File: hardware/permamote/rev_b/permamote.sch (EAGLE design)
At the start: 124 parts, among them J1 TC2030-JLINK-NL, J5 MICRO_USB_B_HIROSE_ZX62R-B-5P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, Q1 PMDXB950UPEL, Q10 PMDXB950UPEL, Q2 PMDXB950UPEL, Q3 PMDXB950UPEL, Q4 PMDXB950UPEL, Q5 PMDXB950UPEL, Q6 PMDXB950UPEL, Q7 PMDXB950UPEL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

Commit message: add mpn, a few nits
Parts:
- R6, R7: value 10k -> DNP
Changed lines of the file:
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@@
 <?xml version="1.0" encoding="utf-8"?>
 <!DOCTYPE eagle SYSTEM "eagle.dtd">
-<eagle version="9.0.1">
+<eagle version="9.0.0">
 <drawing>
 <settings>
@@
 <attributes>
 <attribute name="AUTHOR" value="NEAL JACKSON"/>
-<attribute name="REV" value="A"/>
-<attribute name="TITLE" value="MOTE"/>
+<attribute name="REV" value="B"/>
+<attribute name="TITLE" value="PERMAMOTE"/>
 </attributes>
 <variantdefs>
@@
 </part>
 <part name="GND12" library="supply1" library_urn="urn:adsk.eagle:library:371" deviceset="GND" device=""/>
-<part name="R6" library="passives" deviceset="RESISTOR" device="0402_RES" value="10k">
+<part name="R6" library="passives" deviceset="RESISTOR" device="0402_RES" value="DNP">
 <attribute name="DIGIKEY" value="311-10KJRCT-ND "/>
 <attribute name="MPN" value="RC0402JR-0710KL"/>
@@
 <part name="P+8" library="supply1" library_urn="urn:adsk.eagle:library:371" deviceset="VCC" device=""/>
 <part name="P+1" library="supply1" library_urn="urn:adsk.eagle:library:371" deviceset="VCC" device=""/>
-<part name="R7" library="passives" deviceset="RESISTOR" device="0402_RES" value="10k">
+<part name="R7" library="passives" deviceset="RESISTOR" device="0402_RES" value="DNP">
 <attribute name="DIGIKEY" value="311-10KJRCT-ND "/>
 <attribute name="MPN" value="RC0402JR-0710KL"/>
@@
 <text x="185.42" y="101.6" size="1.778" layer="98">Note: Only populate one type of battery holder</text>
 <text x="2.54" y="182.88" size="5.08" layer="97">Power Supply</text>
-<wire x1="0" y1="68.58" x2="104.14" y2="68.58" width="0.254" layer="94" style="shortdash"/>
-<wire x1="104.14" y1="68.58" x2="104.14" y2="0" width="0.254" layer="94" style="shortdash"/>
+<wire x1="0" y1="71.12" x2="104.14" y2="71.12" width="0.254" layer="94" style="shortdash"/>
+<wire x1="104.14" y1="71.12" x2="104.14" y2="0" width="0.254" layer="94" style="shortdash"/>
 <text x="2.54" y="66.04" size="2.54" layer="97">Boost Regulator</text>
 <text x="124.46" y="53.34" size="1.778" layer="98" rot="R90" align="bottom-center">Divider for Lithium Titanate</text>

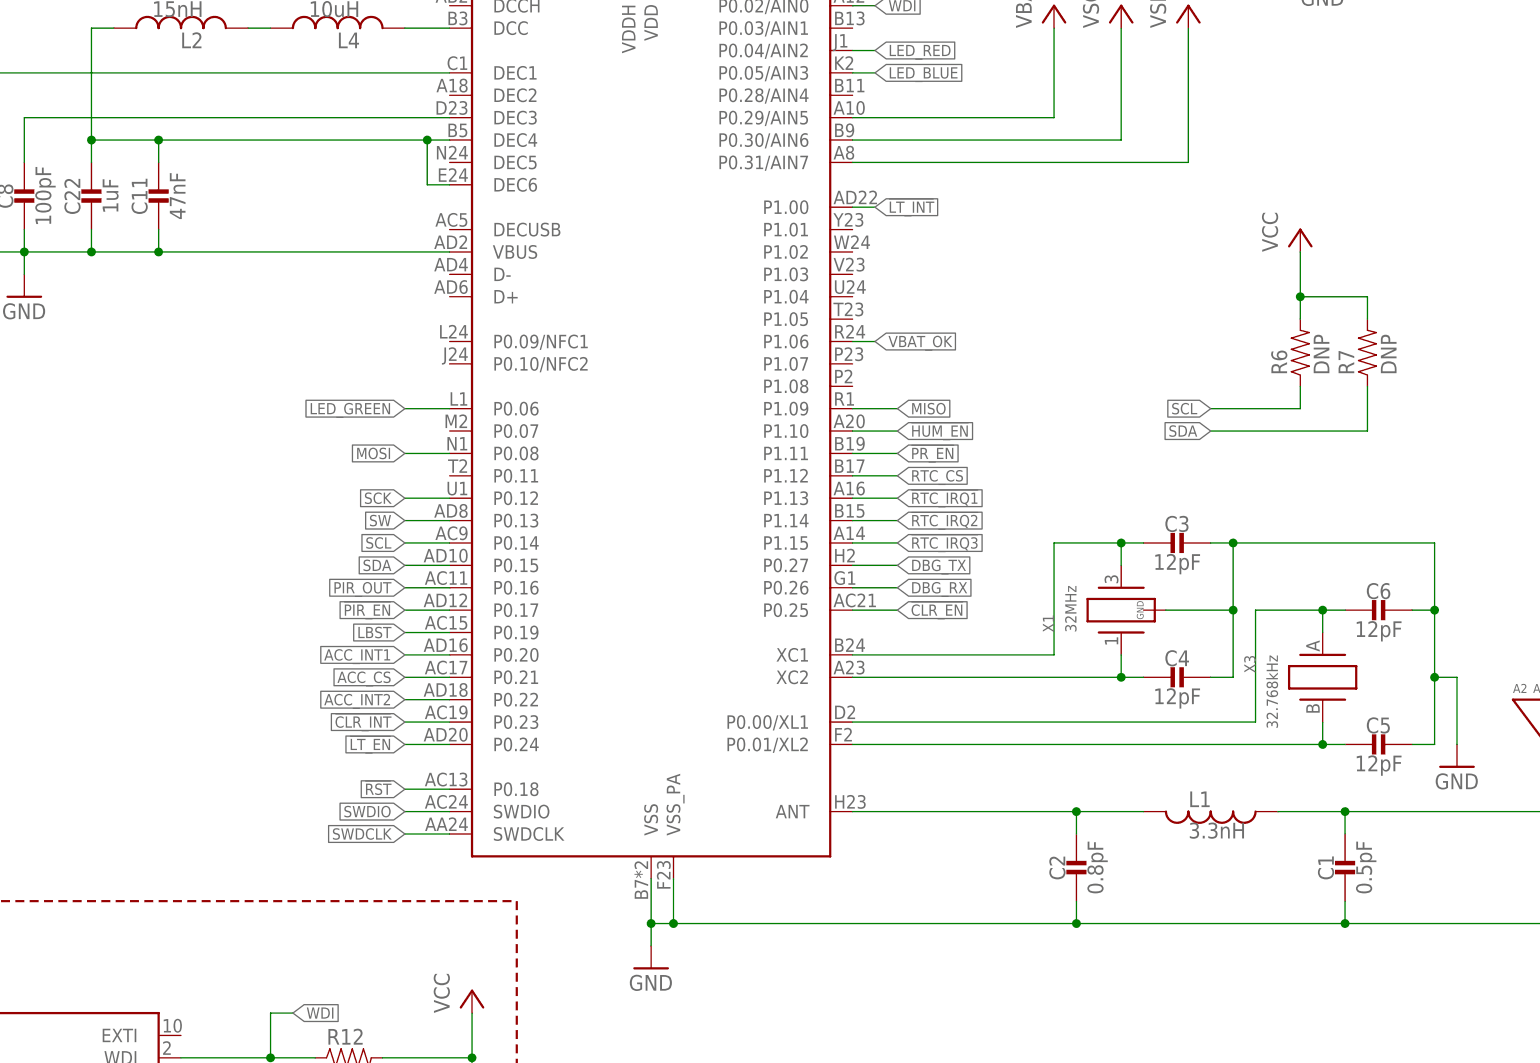
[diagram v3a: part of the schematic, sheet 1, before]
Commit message: Update to nrf52840 v1.0 spec
Add decoupling cap to DEC5
Change values of RF passives
mentioned in #3
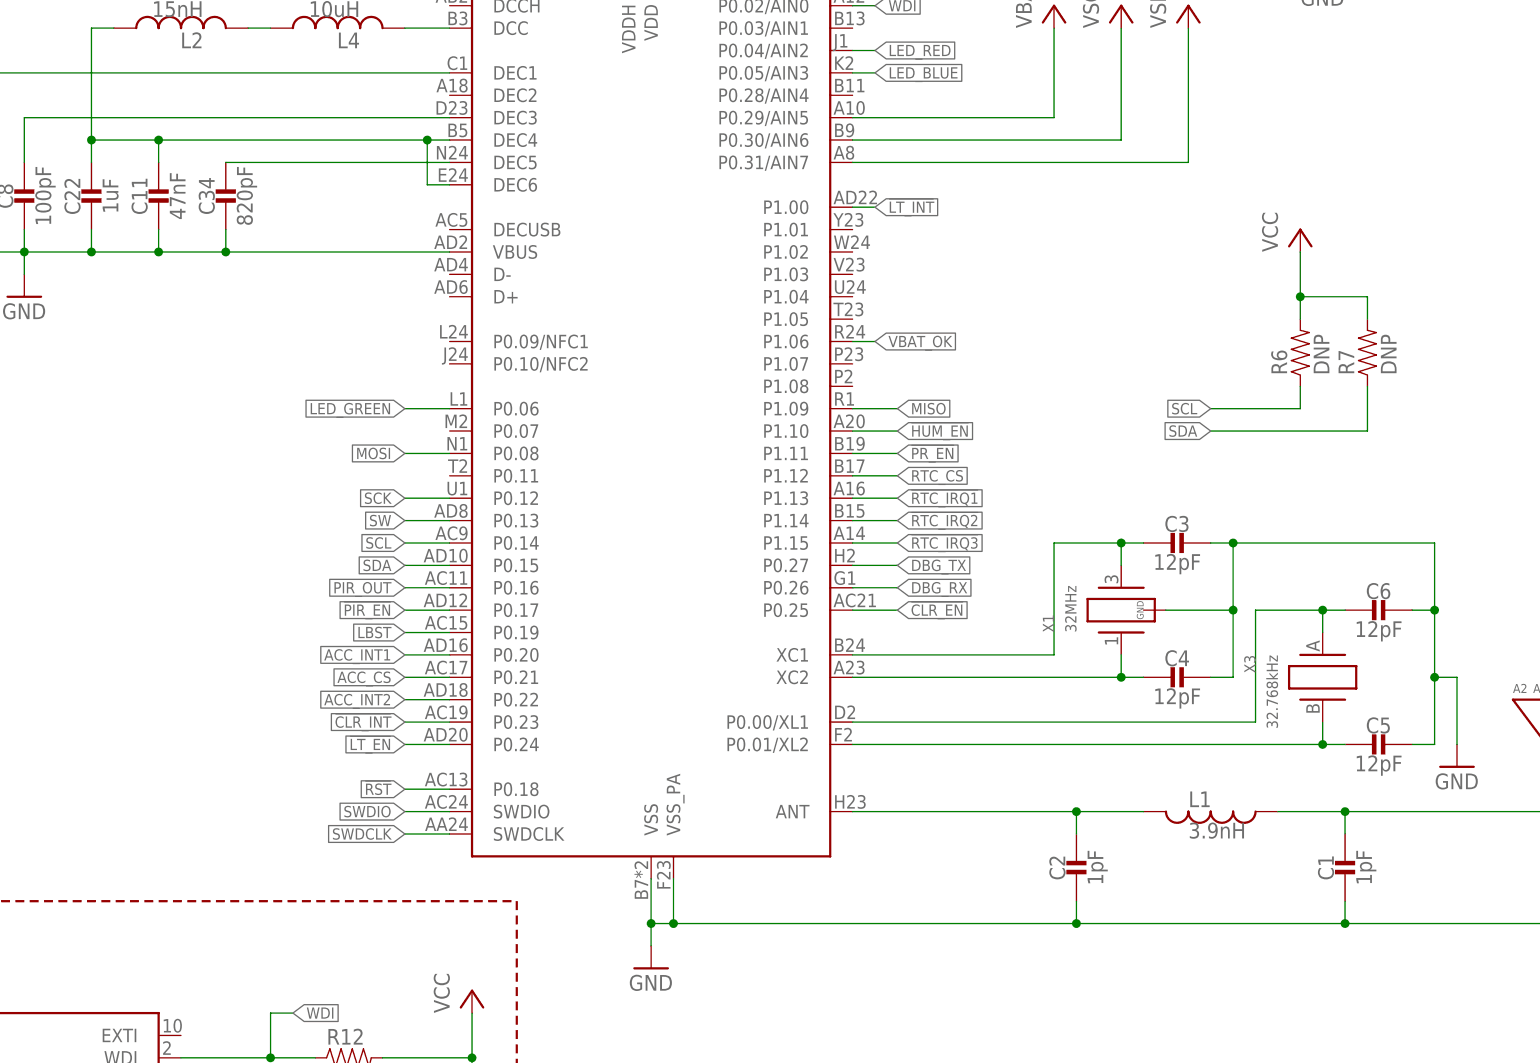
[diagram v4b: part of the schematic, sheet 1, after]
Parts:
- added C34: 820pF, passives:CAPACITOR0402_CAP
- C1: value 0.5pF -> 1pF; DIGIKEY 490-6264-1-ND -> 1276-1595-1-ND; MPN GRM1555C1HR50WA01D -> CL05C010CB5NNNC
- C2: value 0.8pF -> 1pF; DIGIKEY 490-6269-1-ND -> 1276-1595-1-ND; MPN GRM1555C1HR80BA01D -> CL05C010CB5NNNC
- L1: value 3.3nH -> 3.9nH; DIGIKEY 535-10426-1-ND -> 490-1131-1-ND; MPN AISC-0402-3N3J-T -> LQP15MN3N9B02D
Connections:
- new net N$1: C34.1, U10.DEC5
- net GND: now also C34.2
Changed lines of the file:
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@@
 <?xml version="1.0" encoding="utf-8"?>
 <!DOCTYPE eagle SYSTEM "eagle.dtd">
-<eagle version="9.0.0">
+<eagle version="9.0.1">
 <drawing>
 <settings>
@@
 <attribute name="MPN" value="GRM1555C1H120GA01D "/>
 </part>
-<part name="C2" library="passives" deviceset="CAPACITOR" device="0402_CAP" value="0.8pF">
-<attribute name="DIGIKEY" value="490-6269-1-ND"/>
-<attribute name="MPN" value="GRM1555C1HR80BA01D "/>
-</part>
-<part name="C1" library="passives" deviceset="CAPACITOR" device="0402_CAP" value="0.5pF">
-<attribute name="DIGIKEY" value="490-6264-1-ND"/>
-<attribute name="MPN" value="GRM1555C1HR50WA01D "/>
-</part>
-<part name="L1" library="passives" deviceset="INDUCTOR" device="0402" value="3.3nH">
-<attribute name="DIGIKEY" value="535-10426-1-ND"/>
-<attribute name="MPN" value="AISC-0402-3N3J-T "/>
+<part name="C2" library="passives" deviceset="CAPACITOR" device="0402_CAP" value="1pF">
+<attribute name="DIGIKEY" value="1276-1595-1-ND"/>
+<attribute name="MPN" value="CL05C010CB5NNNC"/>
+</part>
+<part name="C1" library="passives" deviceset="CAPACITOR" device="0402_CAP" value="1pF">
+<attribute name="DIGIKEY" value="1276-1595-1-ND"/>
+<attribute name="MPN" value="CL05C010CB5NNNC"/>
+</part>
+<part name="L1" library="passives" deviceset="INDUCTOR" device="0402" value="3.9nH">
+<attribute name="DIGIKEY" value="490-1131-1-ND"/>
+<attribute name="MPN" value="LQP15MN3N9B02D"/>
 </part>
 <part name="X1" library="crystals" deviceset="7V" device="-32.000MAHV-T" value="32MHz"/>
@@
 <part name="TP27" library="headers" deviceset="TEST-POINT" device=""/>
 <part name="U12" library="chips" deviceset="TCS34725" device=""/>
+<part name="C34" library="passives" deviceset="CAPACITOR" device="0402_CAP" value="820pF">
+<attribute name="DIGIKEY" value="1276-6535-1-ND"/>
+<attribute name="MPN" value="CL05B821KO5NNNC"/>
+</part>
 </parts>
 <sheets>
@@
 <instance part="P+16" gate="VCC" x="7.62" y="48.26"/>
 <instance part="P+18" gate="VCC" x="116.84" y="48.26"/>
+<instance part="C34" gate="G$1" x="88.9" y="139.7">
+<attribute name="DIGIKEY" x="88.9" y="139.7" size="1.778" layer="96" display="off"/>
+<attribute name="MPN" x="88.9" y="139.7" size="1.778" layer="96" display="off"/>
+</instance>
 </instances>
 <busses>
@@
 <pinref part="GND3" gate="1" pin="GND"/>
 <pinref part="U10" gate="G$1" pin="VBUS"/>
-<wire x1="114.3" y1="132.08" x2="81.28" y2="132.08" width="0.1524" layer="91"/>
+<wire x1="114.3" y1="132.08" x2="88.9" y2="132.08" width="0.1524" layer="91"/>
 <junction x="73.66" y="132.08"/>
 <pinref part="C11" gate="G$1" pin="2"/>
+<wire x1="88.9" y1="132.08" x2="81.28" y2="132.08" width="0.1524" layer="91"/>
 <wire x1="81.28" y1="132.08" x2="73.66" y2="132.08" width="0.1524" layer="91"/>
 <wire x1="81.28" y1="134.62" x2="81.28" y2="132.08" width="0.1524" layer="91"/>
 <junction x="81.28" y="132.08"/>
+<pinref part="C34" gate="G$1" pin="2"/>
+<wire x1="88.9" y1="134.62" x2="88.9" y2="132.08" width="0.1524" layer="91"/>
+<junction x="88.9" y="132.08"/>
 </segment>
 <segment>
@@
 </segment>
 </net>
+<net name="N$1" class="0">
+<segment>
+<pinref part="U10" gate="G$1" pin="DEC5"/>
+<wire x1="114.3" y1="142.24" x2="88.9" y2="142.24" width="0.1524" layer="91"/>
+<pinref part="C34" gate="G$1" pin="1"/>
+</segment>
+</net>

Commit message: quote out to quickturn
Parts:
- C11: value 47nF -> 10nF; DIGIKEY 445-1264-1-ND -> 490-4516-1-ND; MPN C1005X7R1C473K050BC -> GRM155R71H103KA88D
- C12: value 0.1uF -> 47nF; DIGIKEY 490-6328-1-ND -> 445-1264-1-ND; MPN GRM155R71C104KA88J -> C1005X7R1C473K050BC
- C21: value 1uF -> 0.1uF; DIGIKEY 490-7195-1-ND -> 490-6328-1-ND; MPN GRM155R70G105KA12D -> GRM155R71C104KA88J
- C26: value 4.7uF -> 1uF; DIGIKEY 445-5947-1-ND -> 490-7195-1-ND; MPN C1005X5R0J475K050BC -> GRM155R70G105KA12D
- C29: value 10uF -> 4.7uF; device passives:CAPACITOR0603_CAP -> passives:CAPACITOR0402_CAP; DIGIKEY 490-3896-1-ND -> 445-5947-1-ND; MPN GRM188R60J106ME47D -> C1005X5R0J475K050BC
- C32: value DNP -> 10uF; device passives:CAPACITOR0402_CAP -> passives:CAPACITOR0603_CAP; DIGIKEY (none) -> 490-3896-1-ND; MPN (none) -> GRM188R60J106ME47D
- C34: value 820pF -> DNP; DIGIKEY 1276-6535-1-ND -> (none); MPN CL05B821KO5NNNC -> (none)
- C9: value 10nF -> 820pF; DIGIKEY 490-4516-1-ND -> 1276-6535-1-ND; MPN GRM155R71H103KA88D -> CL05B821KO5NNNC
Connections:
- net N$1: now also C9.1; no longer C34.1
- net N$13: now also C21.1; no longer C20.1
- net N$2: now also C15.1; no longer C14.1
- net N$26: now also C33.1; no longer C32.1
- net N$27: now also C34.1; no longer C33.1
- net N$3: now also C12.1, C23.1; no longer C11.1, C22.1
- net N$5: now also C1.1; no longer C2.1
- net N$6: now also C2.1; no longer C1.1
- net VCC: now also C14.1, C20.1, C22.1, C27.1, C32.1; no longer C12.1, C15.1, C21.1, C23.1, C30.1
- net VOC_SAMP_VSTOR: now also C11.1, C28.1; no longer C10.1, C27.1
- net VREF_SAMP: now also C10.1; no longer C9.1
- net VSOL: now also C29.1; no longer C28.1
- net VSW: now also C30.1; no longer C29.1
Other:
- moved on the sheet: C1, C10, C12, C13, C14, C15, C17, C18, C19, C2, C22, C24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
